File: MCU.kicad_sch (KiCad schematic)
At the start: 30 parts, among them J1 USB_B_Micro, J2 Conn_01x02, J4 Debugger Pins, J6 GPIO, U1 NCP1117-3.3_SOT223, U2 W25Q128JVS, U3 RP2040, Y1 ABLS-12.000MHZ-B4-T

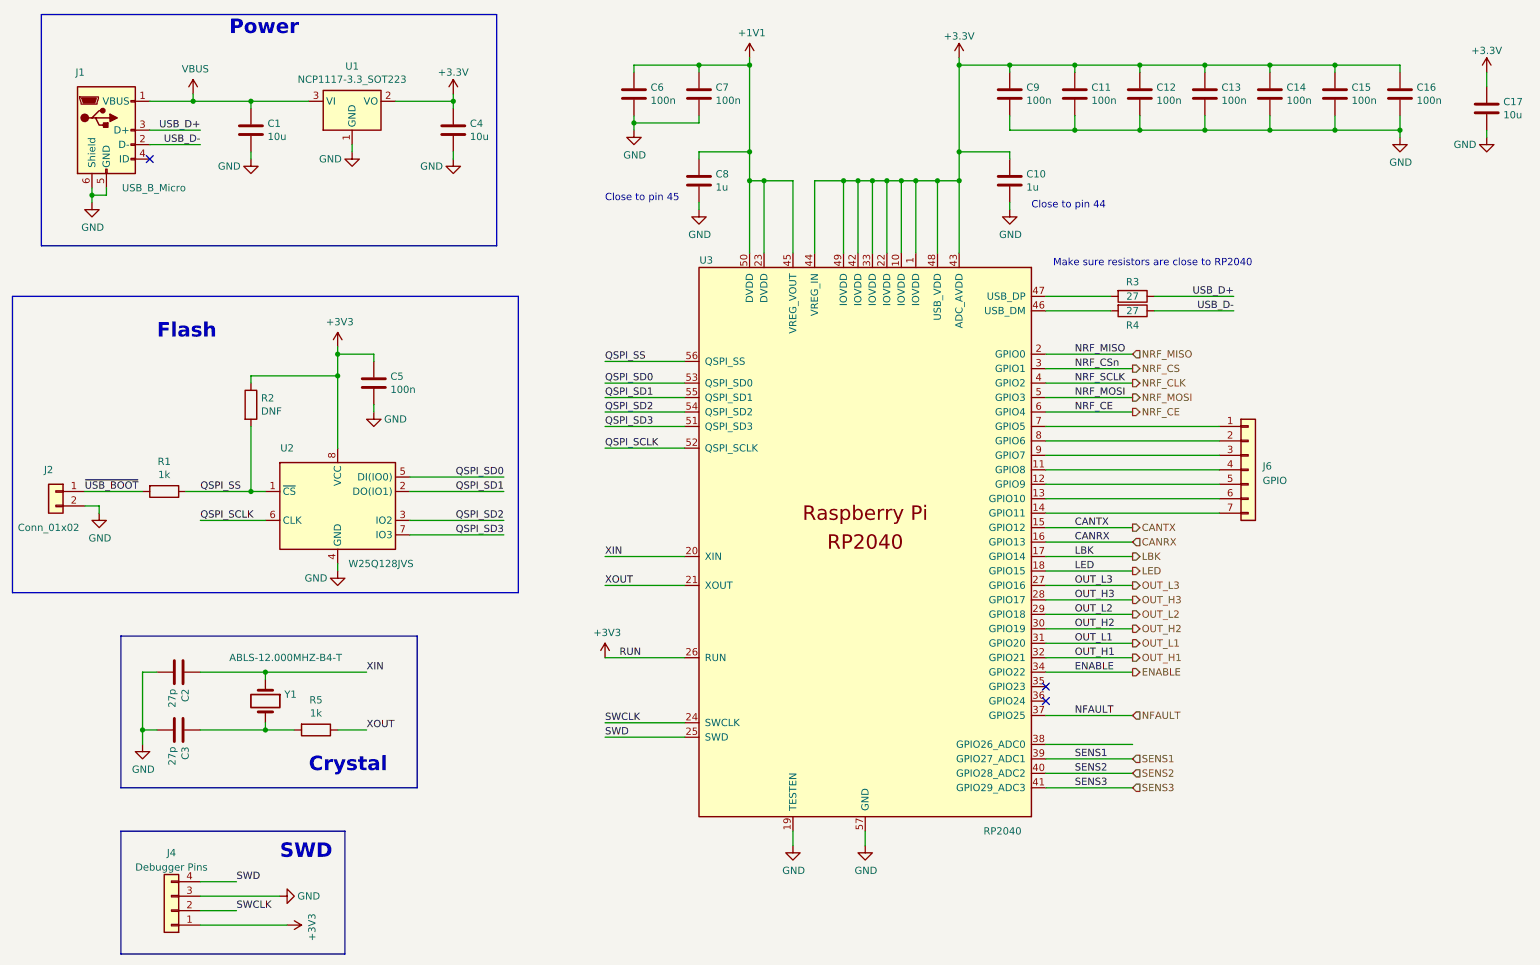
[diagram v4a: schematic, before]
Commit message: Re-annotate all components
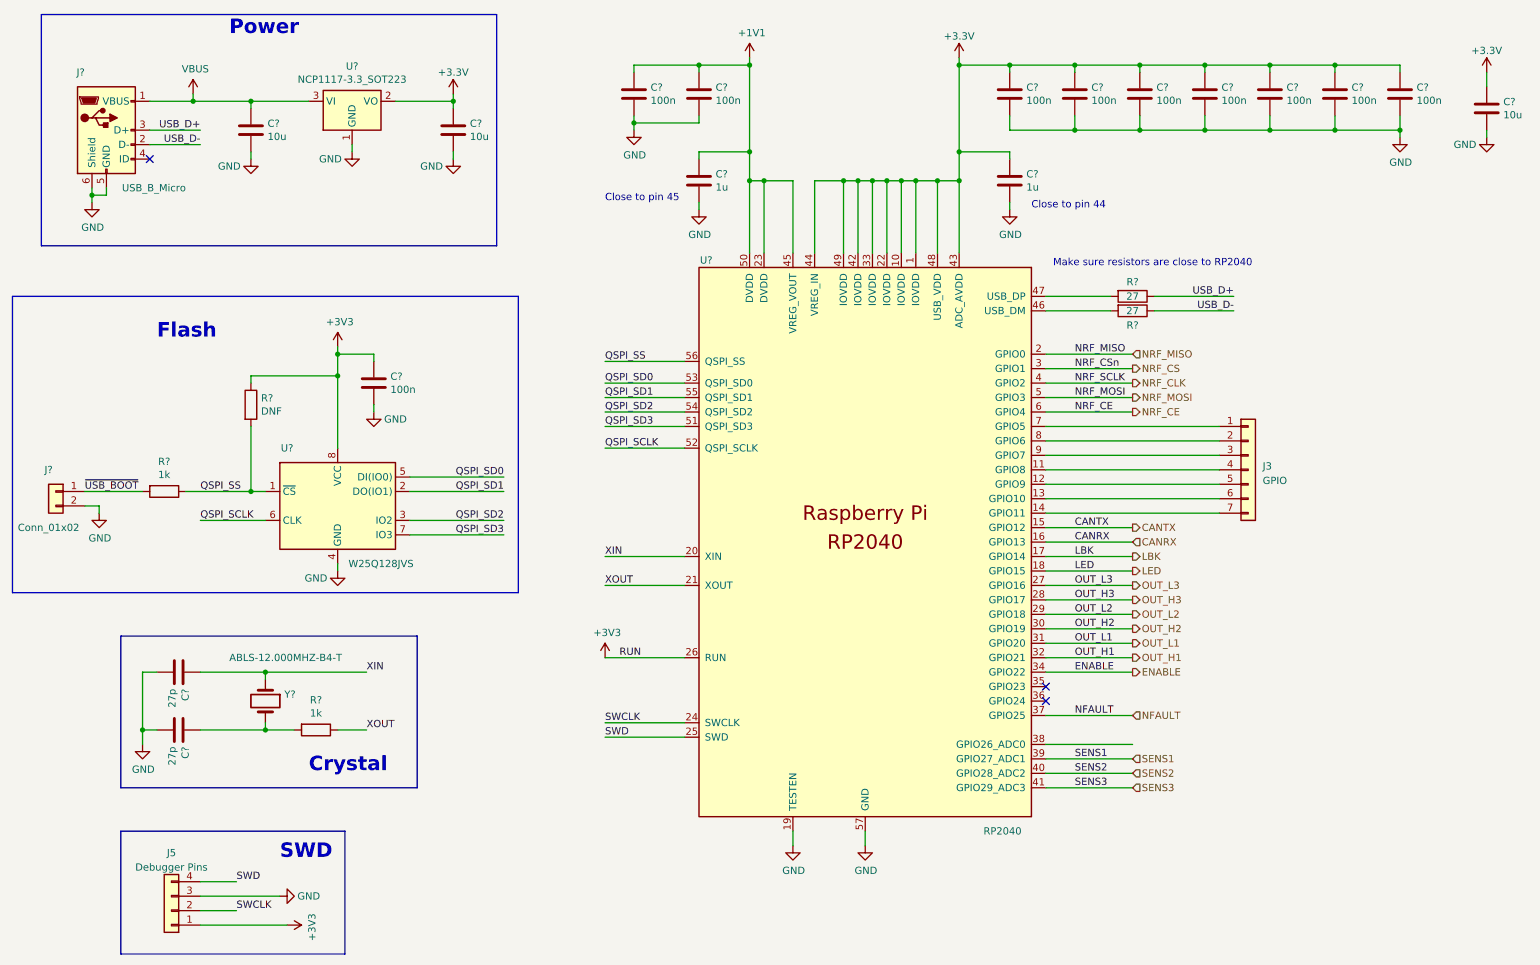
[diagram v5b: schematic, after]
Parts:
- renumbered C13 to C?, C2 to C?, C14 to C?, C17 to C?, C3 to C?, C7 to C?, C16 to C?, C12 to C?, C15 to C?, C4 to C?, C5 to C?, C1 to C?, C9 to C?, C6 to C?, C11 to C?, C8 to C?, C10 to C?, J6 to J3, J4 to J5, J1 to J?, J2 to J?, R2 to R?, R3 to R?, R1 to R?, R4 to R?, R5 to R?, U1 to U?, U3 to U?, U2 to U?, Y1 to Y?
